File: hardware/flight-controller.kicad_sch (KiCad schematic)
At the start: 117 parts, among them J1 USB_C_Receptacle_USB2.0_16P, J10 Screw_Terminal_01x02, J11 Micro_SD_Card_Det_Hirose_DM3AT, J12 Conn_01x03, J13 Conn_01x03, J14 Conn_01x03, J15 Conn_01x03, J16 Screw_Terminal_01x02, J17 Conn_01x04, J18 Screw_Terminal_01x02, J19 Conn_01x02, J2 Conn_01x02, J20 Conn_01x02, J21 Conn_01x02, J22 Conn_01x02, J23 Conn_01x02, J3 Conn_Coaxial, J4 Conn_01x04, J5 Screw_Terminal_01x02, J6 Conn_01x04, J7 Screw_Terminal_01x02, J8 Conn_01x04, J9 Screw_Terminal_01x02, U1 BMP384, U2 LSM6DSOTR, U3 MMC5983MA, U4 NEO-M9N, U5 TPS2121RUXR, U6 AP62300TWU, U7 STM32H723VGTx, Y1 Q13FC13500004, Y2 X322525MOB4SI

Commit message: added lines to schematic
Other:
- note added: "Accelerometer/Gyroscope"
- note added: "Buck Regulator"
- note added: "Buttons"
- note added: "Buzzer"
- note added: "Debug Header"
- note added: "ESC Headers"
- note added: "ESC Power Terminals"
- note added: "GNSS Module"
- note added: "I2C Headers"
- note added: "Magnetometer"
- note added: "Micro SD Connector"
- note added: "Microcontroller"
- note added: "Oscillators"
- note added: "Power MUX"
- note added: "Power Terminals"
- note added: "Pressure Sensor"
- note added: "Status LEDs"
- note added: "UART Connectors"
- note added: "USB C Connector"
- moved on the sheet: BOOT1, BT1, BZ1, C1, C10, C11, C12, C13, C14, C16, C18, C19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

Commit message: added production files
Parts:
- R6, R8: footprint Resistor_SMD:R_0402_1005Metric -> Resistor_SMD:R_0603_1608Metric

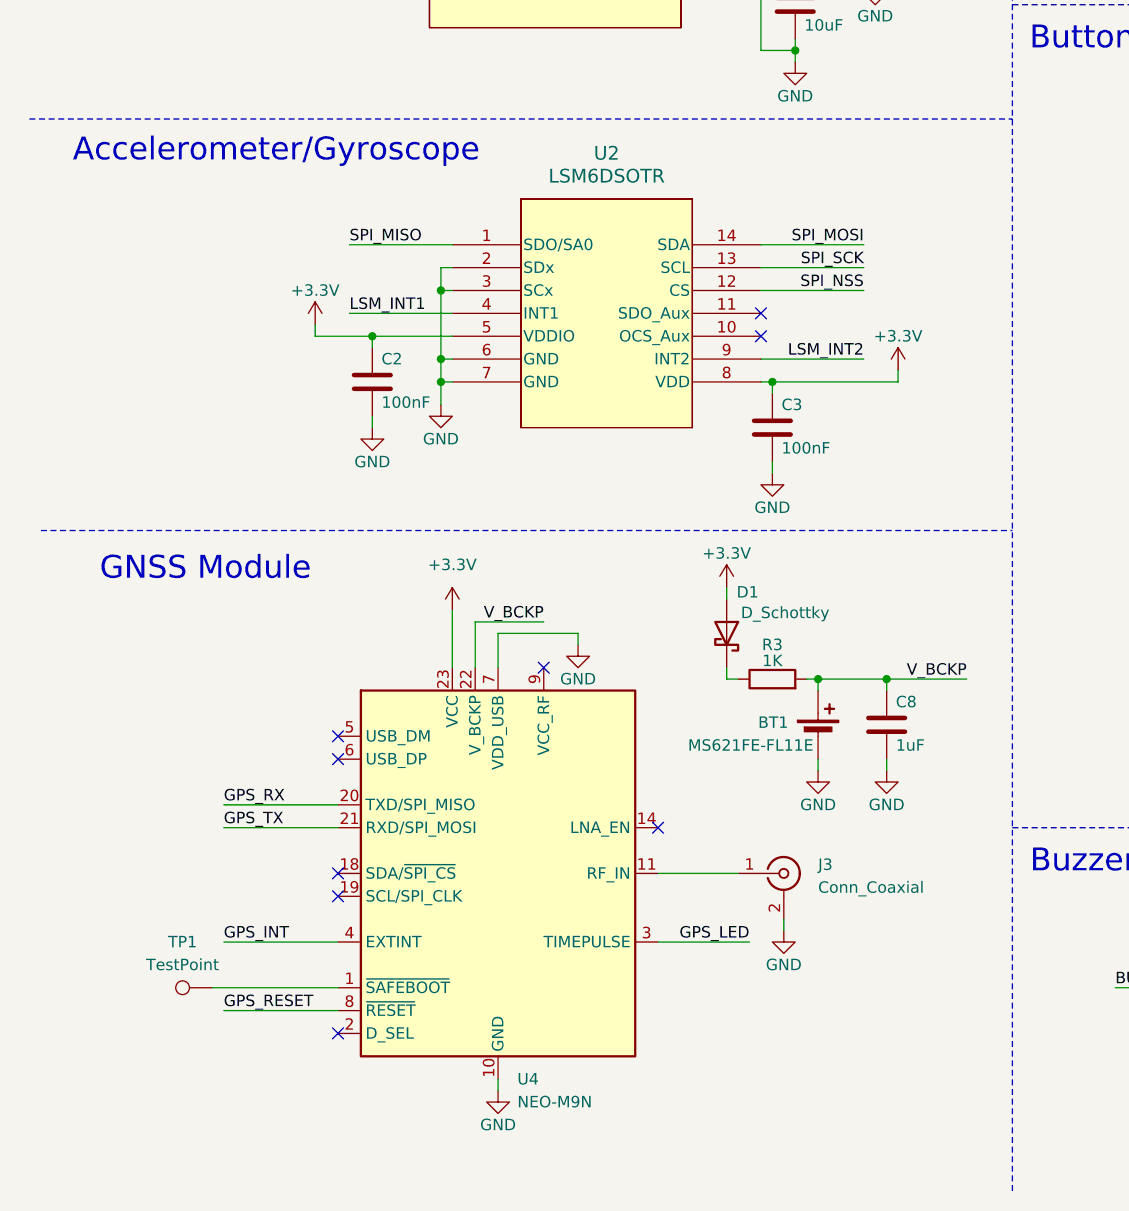
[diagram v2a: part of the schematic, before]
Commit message: replaced gps with max-m10s
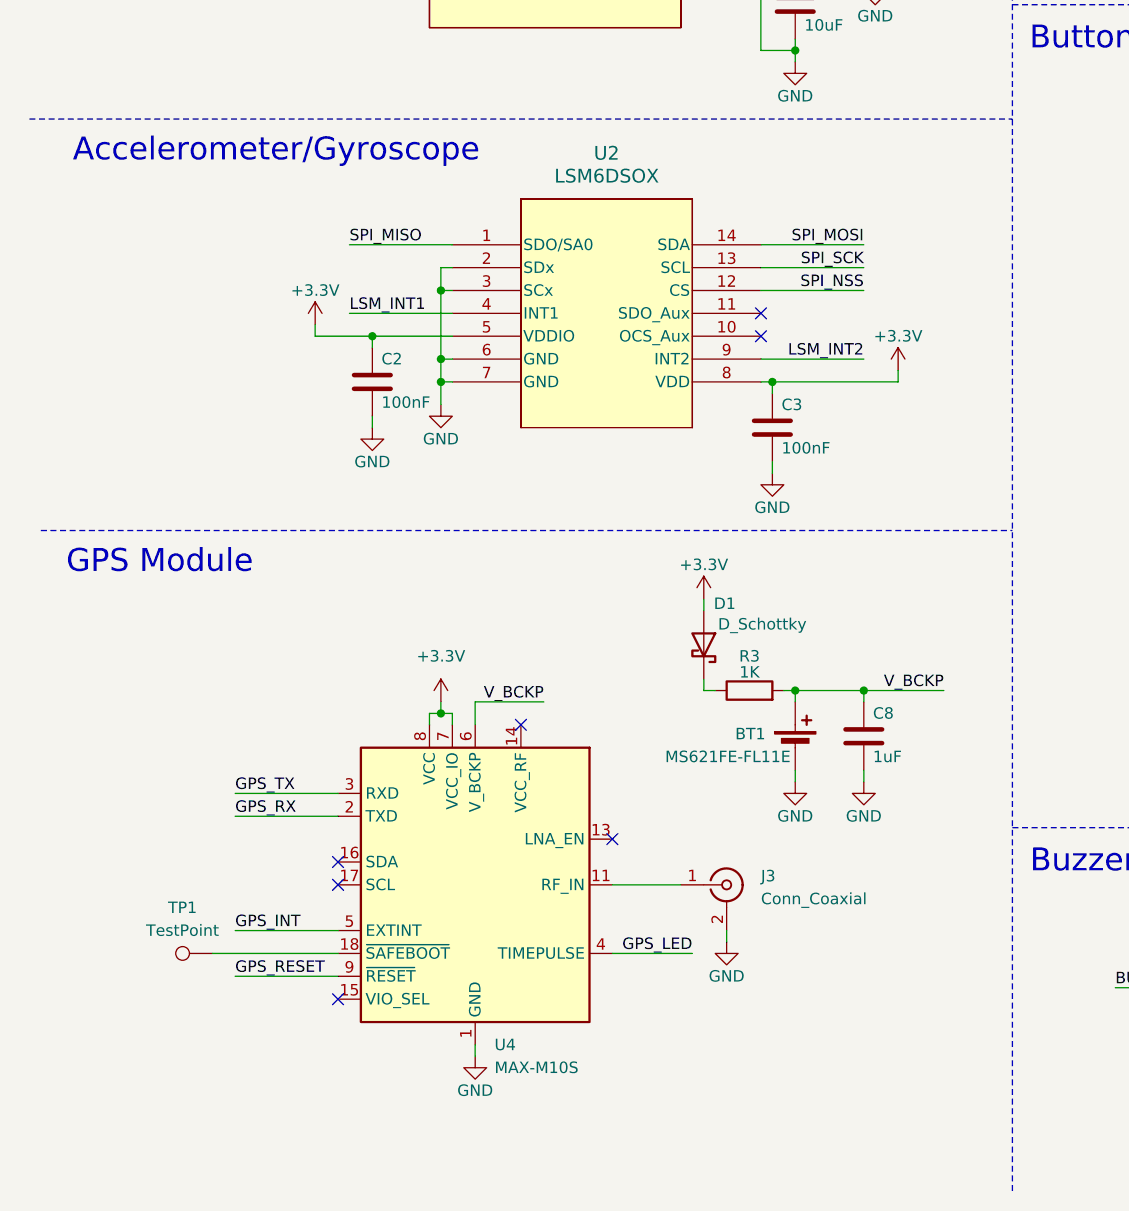
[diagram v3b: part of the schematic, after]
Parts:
- removed U4: NEO-M9N, RF_GPS:ublox_NEO, symbol RF_GPS:NEO-M9N
- added U4: MAX-M10S, RF_GPS:ublox_MAX, symbol RF_GPS:MAX-M10S
- U2: value LSM6DSOTR -> LSM6DSOX
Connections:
- net +3.3V: now also U4.7 (VCC_IO), U4.8 (VCC)
- net GND: now also U4.1 (GND), U4.10 (GND), U4.12 (GND)
- net GPS_INT: now also U4.5 (EXTINT)
- net GPS_LED: now also U4.4 (TIMEPULSE)
- net GPS_RESET: now also U4.9 (~{RESET})
- net GPS_RX: now also U4.2 (TXD)
- net GPS_TX: now also U4.3 (RXD)
- net V_BCKP: now also U4.6 (V_BCKP)
- net at TP1.1: now also U4.18 (~{SAFEBOOT})
- net at J3.1 (In): now also U4.11 (RF_IN)
- no-connect marks 51 -> 49
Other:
- note added: "GPS Module"
- note removed: "GNSS Module"
- moved on the sheet: BT1, C8, D1, J3, R3, TP1
